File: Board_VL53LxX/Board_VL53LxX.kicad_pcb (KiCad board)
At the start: 2 copper layers, 15 x 16 mm, 12 parts, among them J1 Conn_01x06, U1 VL53L0X

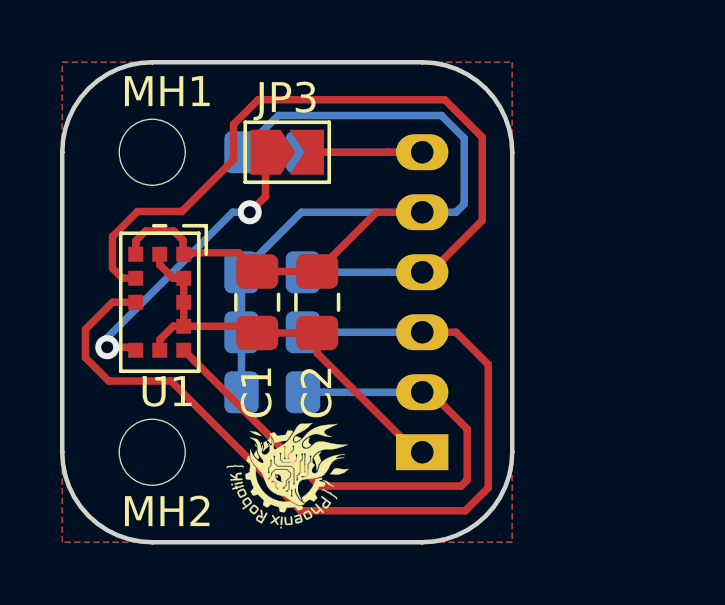
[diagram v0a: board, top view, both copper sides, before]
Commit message: Update VL53L0X PCB
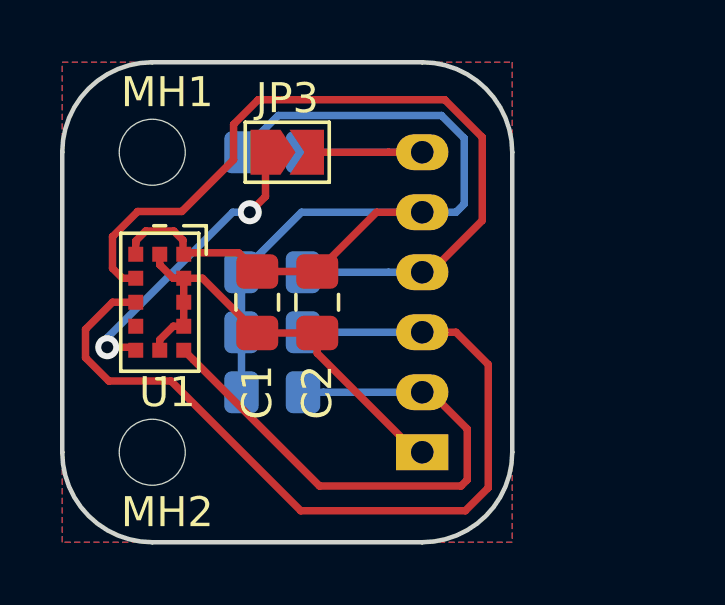
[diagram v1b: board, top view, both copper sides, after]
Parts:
- removed REF**: Logo_5,1mm, PhoenixRobotik:Logo_5,1mm
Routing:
- net GND: track 14.4 -> 15.0 mm

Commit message: Changed JST connectors
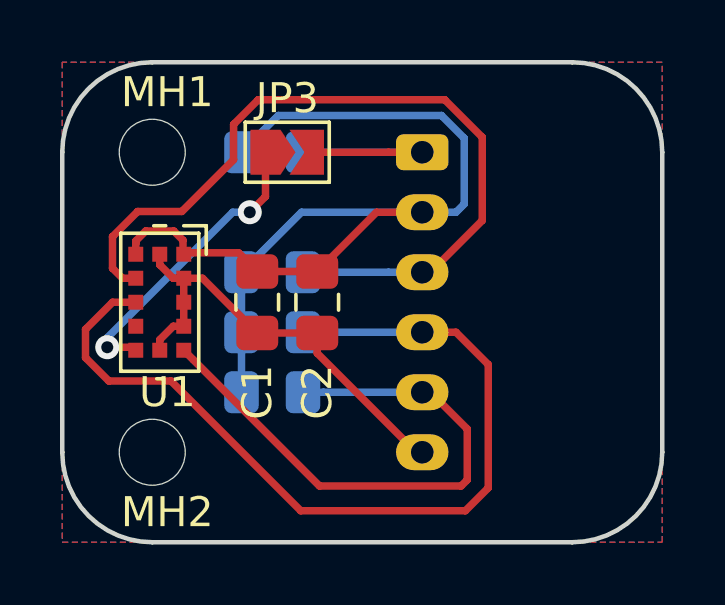
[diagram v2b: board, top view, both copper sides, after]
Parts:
- J1: footprint Connector_JST:JST_PH_B6B-PH-K_1x06_P2.00mm_Vertical -> Connector_JST:JST_PH_S6B-PH-K_1x06_P2.00mm_Horizontal
- moved J1 10.0 mm to (112.0, 83.0), turned to 270 degrees
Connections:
- J1 pad 1: GND -> /GPIO
- J1 pad 2: /~XSHUT -> +2V8
- J1 pad 3: /I2C_SDA -> /I2C_SCL
- J1 pad 4: /I2C_SCL -> /I2C_SDA
- J1 pad 5: +2V8 -> /~XSHUT
- J1 pad 6: /GPIO -> GND
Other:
- board size 15 x 16 mm -> 20 x 16 mm

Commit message: update board
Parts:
- added LOGO1: Logo_Open_Hardware_Small, Symbol:OSHW-Logo2_7.3x6mm_SilkScreen, B.Cu at (107.6, 93.2)
- added LOGO2: Logo_Open_Hardware_Small, PhenixRobotik:Logo_8,5mm, B.Cu at (107.8, 84.4)
- MH1, MH2: value MountingHole -> MountingHole_Pad; footprint MountingHole:MountingHole_2.2mm_M2 -> MountingHole:MountingHole_2.2mm_M2_Pad
- R1, R2, R3, R4: moved to F.Cu
- U1: footprint PhoenixRobotik:TOF-12_4.4x2.4x1.0mm_P0.8mm -> PhenixRobotik:TOF-12_4.4x2.4x1.0mm_P0.8mm
- moved J1 11.4 mm to (117.4, 93.0), turned to 90 degrees
- moved R2 8.43 mm to (114.8, 90.2), turned to 90 degrees
- moved R3 5.97 mm to (108.4, 85.2), turned to 180 degrees
- moved R1 5.60 mm to (112.6, 88.8), turned to 270 degrees
- moved R4 4.44 mm to (111.4, 83.6), turned to 90 degrees
- moved C1 3.20 mm to (107.6, 91.0)
- moved C2 3.20 mm to (109.6, 91.0)
- moved JP3 0.92 mm to (108.4, 82.8)
- moved U1 0.25 mm to (103.0, 88.0), turned to 270 degrees
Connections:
- MH1 pad 1: (no net) -> GND
- MH2 pad 1: (no net) -> GND
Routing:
- net /I2C_SDA: track 29.6 -> 14.0 mm
- net /I2C_SCL: track 26.9 -> 14.1 mm
- net +2V8: track 34.6 -> 24.4 mm, vias 0 -> 2
- net /GPIO: track 7.75 -> 15.7 mm, vias 0 -> 1
- net Net-(JP3-Pad1): track 10.0 -> 5.79 mm, vias 2 -> 0
- net GND: track 15.0 -> 12.0 mm, vias 0 -> 2
- net /~XSHUT: track 19.1 -> 16.3 mm, vias 0 -> 2
- net (no net): vias 0 -> 1
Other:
- board text added: "PhenixRobotik"

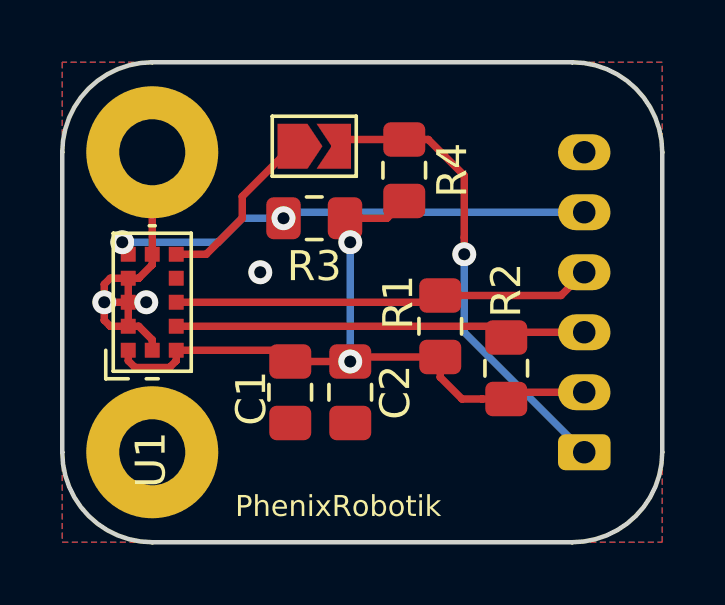
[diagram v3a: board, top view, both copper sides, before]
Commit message: Changed connector orientation, better capacitance positionning, cleaner pcb
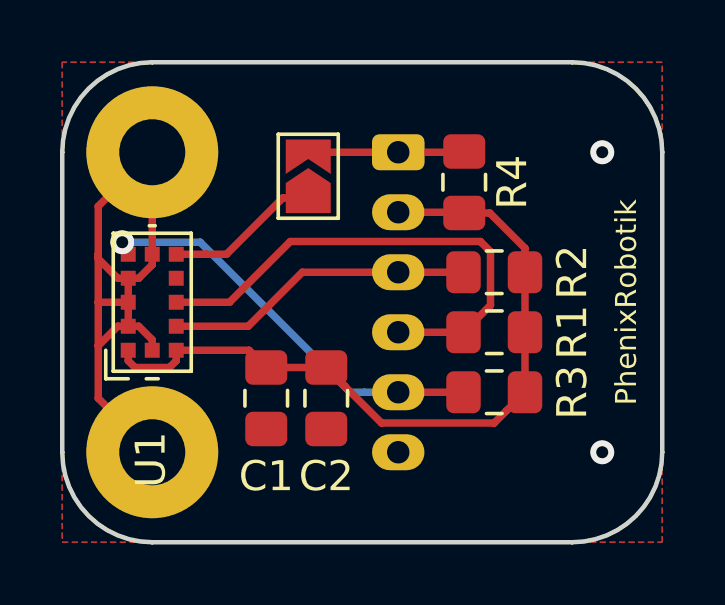
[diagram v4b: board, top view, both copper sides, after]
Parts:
- moved J1 11.8 mm to (111.2, 83.0), turned to 270 degrees
- moved R3 8.35 mm to (114.4, 91.0)
- moved LOGO2 3.26 mm to (107.2, 87.6)
- moved R2 3.22 mm to (114.4, 87.0), turned to 180 degrees
- moved R4 2.04 mm to (113.4, 84.0)
- moved R1 1.81 mm to (114.4, 89.0), turned to 0 degrees
- moved JP3 1.02 mm to (108.2, 83.8), turned to 90 degrees
- moved C1 0.82 mm to (106.8, 91.2)
- moved C2 0.82 mm to (108.8, 91.2)
- moved LOGO1 0.20 mm to (107.8, 93.2)
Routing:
- net GND: track 12.0 -> 22.9 mm
- net /GPIO: track 15.7 -> 5.24 mm, vias 1 -> 0
- net /I2C_SCL: track 14.1 -> 10.3 mm
- net /I2C_SDA: track 14.0 -> 16.7 mm
- net /~XSHUT: track 16.3 -> 13.9 mm, vias 2 -> 1
- net +2V8: track 24.4 -> 25.1 mm, vias 2 -> 0
- net Net-(JP3-Pad1): track 5.79 -> 5.18 mm
- net (no net): vias 1 -> 0
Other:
- board text removed: "+2V8"
- board text removed: "GND"
